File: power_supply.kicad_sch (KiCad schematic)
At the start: 46 parts, among them J3 JST_SH_1x4_SM04B-SRSS-TB-LF-SN, Q2 DMG1012T-7, U8 MPM54304GMN-0001, U9 LT3033EUDC_QFN

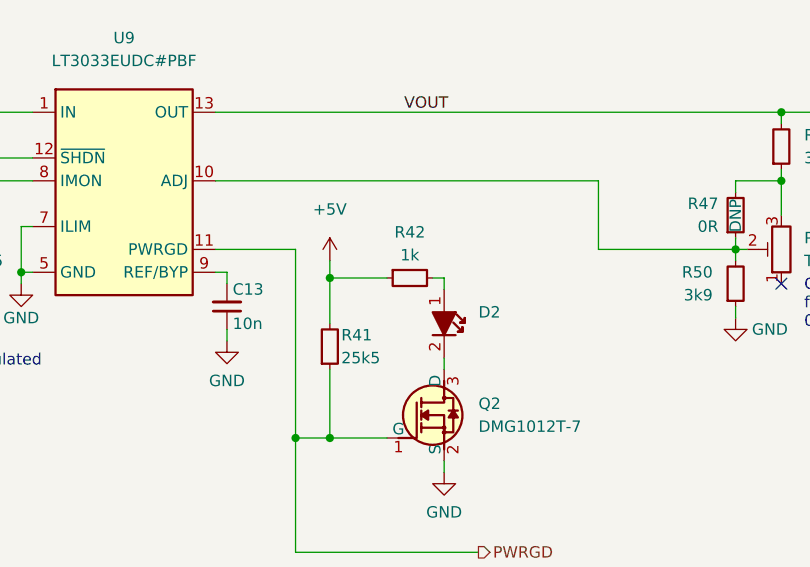
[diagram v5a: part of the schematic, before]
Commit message: [#52835] schematics: update translators pinout to for better package breakout
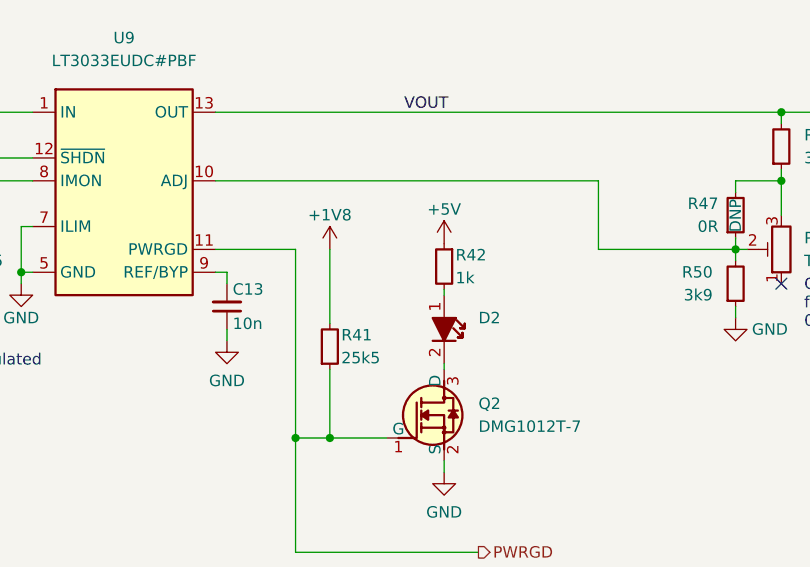
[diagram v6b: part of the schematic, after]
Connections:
- net +1V8: now also R41.2
- net +5V: no longer R41.2
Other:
- moved on the sheet: D2, R42
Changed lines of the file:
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@@
   (junction (at 189.23 186.055) (diameter 0) (color 0 0 0 0)
   )
-  (junction (at 231.14 196.85) (diameter 0) (color 0 0 0 0)
-  )
   (junction (at 241.3 78.74) (diameter 0) (color 0 0 0 0)
   )
@@
     (stroke (width 0) (type default) (color 0 0 0 0))
   )
-  (wire (pts (xy 231.14 194.945) (xy 231.14 196.85))
-    (stroke (width 0) (type default) (color 0 0 0 0))
-  )
   (wire (pts (xy 245.11 104.14) (xy 254 104.14))
     (stroke (width 0) (type default) (color 0 0 0 0))
@@
     (stroke (width 0) (type default) (color 0 0 0 0))
   )
-  (wire (pts (xy 242.57 196.85) (xy 243.84 196.85))
-    (stroke (width 0) (type default) (color 0 0 0 0))
-  )
   (polyline (pts (xy 229.235 55.245) (xy 229.235 66.675))
     (stroke (width 0) (type default) (color 0 0 0 0))
@@
     (stroke (width 0) (type default) (color 0 0 0 0))
   )
-  (wire (pts (xy 231.14 196.85) (xy 237.49 196.85))
-    (stroke (width 0) (type default) (color 0 0 0 0))
-  )
   (wire (pts (xy 180.975 57.785) (xy 180.975 59.055))
     (stroke (width 0) (type default) (color 0 0 0 0))
@@
     (stroke (width 0) (type default) (color 0 0 0 0))
   )
+  (wire (pts (xy 231.14 193.675) (xy 231.14 201.93))
+    (stroke (width 0) (type default) (color 0 0 0 0))
+  )
   (wire (pts (xy 302.26 178.435) (xy 327.66 178.435))
     (stroke (width 0) (type default) (color 0 0 0 0))
@@
     (stroke (width 0) (type default) (color 0 0 0 0))
   )
-  (wire (pts (xy 243.84 205.74) (xy 243.84 207.01))
+  (wire (pts (xy 243.84 206.375) (xy 243.84 207.01))
     (stroke (width 0) (type default) (color 0 0 0 0))
   )
@@
     (stroke (width 0) (type default) (color 0 0 0 0))
   )
-  (wire (pts (xy 231.14 196.85) (xy 231.14 201.93))
-    (stroke (width 0) (type default) (color 0 0 0 0))
-  )
   (wire (pts (xy 193.04 97.79) (xy 194.31 97.79))
     (stroke (width 0) (type default) (color 0 0 0 0))
@@
     (stroke (width 0) (type default) (color 0 0 0 0))
   )
-  (wire (pts (xy 243.84 196.85) (xy 243.84 198.12))
+  (wire (pts (xy 243.84 198.12) (xy 243.84 198.755))
     (stroke (width 0) (type default) (color 0 0 0 0))
   )
@@
     (pin "1")
   )
-  (symbol (lib_id "antmicropower:+5V") (at 231.14 194.945 0) (unit 1)
-    (in_bom yes) (on_board yes) (fields_autoplaced)
-    (property "Reference" "#PWR0212" (id 0) (at 246.38 197.485 0)
+  (symbol (lib_id "antmicropower:+5V") (at 243.84 193.04 0) (unit 1)
+    (in_bom yes) (on_board yes)
+    (property "Reference" "#PWR0212" (id 0) (at 259.08 195.58 0)
       (effects (font (size 1.27 1.27) (thickness 0.15)) (justify left bottom) hide)
     )
-    (property "Value" "+5V" (id 1) (at 231.14 189.23 0)
+    (property "Value" "+5V" (id 1) (at 243.84 189.23 0)
       (effects (font (size 1.27 1.27) (thickness 0.15)))
     )
-    (property "Footprint" "" (id 2) (at 246.38 202.565 0)
+    (property "Footprint" "" (id 2) (at 259.08 200.66 0)
       (effects (font (size 1.27 1.27) (thickness 0.15)) (justify left bottom) hide)
     )
-    (property "Datasheet" "" (id 3) (at 246.38 205.105 0)
+    (property "Datasheet" "" (id 3) (at 259.08 203.2 0)
       (effects (font (size 1.27 1.27) (thickness 0.15)) (justify left bottom) hide)
     )
-    (property "Author" "Antmicro" (id 4) (at 246.38 202.565 0)
+    (property "Author" "Antmicro" (id 4) (at 259.08 200.66 0)
       (effects (font (size 1.27 1.27) (thickness 0.15)) (justify left bottom) hide)
     )
-    (property "License" "Apache-2.0" (id 5) (at 246.38 205.105 0)
+    (property "License" "Apache-2.0" (id 5) (at 259.08 203.2 0)
       (effects (font (size 1.27 1.27) (thickness 0.15)) (justify left bottom) hide)
     )
@@
     (pin "1")
   )
-  (symbol (lib_id "antmicroLEDIndicationDiscrete:LED_G_0603_KP-1608CGCK") (at 243.84 198.12 270) (unit 1)
+  (symbol (lib_id "antmicroLEDIndicationDiscrete:LED_G_0603_KP-1608CGCK") (at 243.84 198.755 270) (unit 1)
     (in_bom yes) (on_board yes) (fields_autoplaced)
-    (property "Reference" "D2" (id 0) (at 247.65 200.6599 90)
+    (property "Reference" "D2" (id 0) (at 247.65 201.2949 90)
       (effects (font (size 1.27 1.27) (thickness 0.15)) (justify left))
     )
-    (property "Value" "LED_G_0603_KP-1608CGCK" (id 1) (at 247.65 203.1999 90)
+    (property "Value" "LED_G_0603_KP-1608CGCK" (id 1) (at 247.65 203.8349 90)
       (effects (font (size 1.27 1.27) (thickness 0.15)) (justify left) hide)
     )
-    (property "Footprint" "antmicro-footprints:LED_0603_1608Metric_G" (id 2) (at 233.68 220.98 0)
+    (property "Footprint" "antmicro-footprints:LED_0603_1608Metric_G" (id 2) (at 233.68 221.615 0)
       (effects (font (size 1.27 1.27) (thickness 0.15)) (justify left bottom) hide)
     )
-    (property "Datasheet" "http://www.farnell.com/datasheets/2045956.pdf" (id 3) (at 231.14 220.98 0)
+    (property "Datasheet" "http://www.farnell.com/datasheets/2045956.pdf" (id 3) (at 231.14 221.615 0)
       (effects (font (size 1.27 1.27) (thickness 0.15)) (justify left bottom) hide)
     )
-    (property "MPN" "KP-1608CGCK" (id 4) (at 228.6 220.98 0)
+    (property "MPN" "KP-1608CGCK" (id 4) (at 228.6 221.615 0)
       (effects (font (size 1.27 1.27) (thickness 0.15)) (justify left bottom) hide)
     )
-    (property "Manufacturer" "Kingbright" (id 5) (at 226.06 220.98 0)
+    (property "Manufacturer" "Kingbright" (id 5) (at 226.06 221.615 0)
       (effects (font (size 1.27 1.27) (thickness 0.15)) (justify left bottom) hide)
     )
-    (property "Author" "Antmicro" (id 6) (at 223.52 220.98 0)
+    (property "Author" "Antmicro" (id 6) (at 223.52 221.615 0)
       (effects (font (size 1.27 1.27) (thickness 0.15)) (justify left bottom) hide)
     )
-    (property "License" "Apache-2.0" (id 7) (at 220.98 220.98 0)
+    (property "License" "Apache-2.0" (id 7) (at 220.98 221.615 0)
       (effects (font (size 1.27 1.27) (thickness 0.15)) (justify left bottom) hide)
     )
@@
     (pin "2")
   )
+  (symbol (lib_id "antmicropower:+1V8") (at 231.14 193.675 0) (unit 1)
+    (in_bom yes) (on_board yes)
+    (property "Reference" "#PWR0270" (id 0) (at 246.38 196.215 0)
+      (effects (font (size 1.27 1.27) (thickness 0.15)) (justify left bottom) hide)
+    )
+    (property "Value" "+1V8" (id 1) (at 231.14 189.865 0)
+      (effects (font (size 1.27 1.27) (thickness 0.15)))
+    )
+    (property "Footprint" "" (id 2) (at 246.38 201.295 0)
+      (effects (font (size 1.27 1.27) (thickness 0.15)) (justify left bottom) hide)
+    )
+    (property "Datasheet" "" (id 3) (at 246.38 203.835 0)
+      (effects (font (size 1.27 1.27) (thickness 0.15)) (justify left bottom) hide)
+    )
+    (property "Author" "Antmicro" (id 4) (at 246.38 201.295 0)
+      (effects (font (size 1.27 1.27) (thickness 0.15)) (justify left bottom) hide)
+    )
+    (property "License" "Apache-2.0" (id 5) (at 246.38 203.835 0)
+      (effects (font (size 1.27 1.27) (thickness 0.15)) (justify left bottom) hide)
+    )
+    (pin "1")
+  )
   (symbol (lib_id "antmicropower:GND") (at 180.975 64.135 0) (unit 1)
     (in_bom yes) (on_board yes)
@@
     (pin "2")
   )
-  (symbol (lib_id "antmicroResistors0402:R_1k_0402") (at 237.49 196.85 0) (unit 1)
+  (symbol (lib_id "antmicroResistors0402:R_1k_0402") (at 243.84 193.04 270) (unit 1)
     (in_bom yes) (on_board yes)
-    (property "Reference" "R42" (id 0) (at 240.03 191.77 0)
-      (effects (font (size 1.27 1.27) (thickness 0.15)))
+    (property "Reference" "R42" (id 0) (at 245.11 194.31 90)
+      (effects (font (size 1.27 1.27) (thickness 0.15)) (justify left))
     )
-    (property "Value" "R_1k_0402" (id 1) (at 257.81 209.55 0)
+    (property "Value" "R_1k_0402" (id 1) (at 231.14 213.36 0)
       (effects (font (size 1.27 1.27) (thickness 0.15)) (justify left bottom) hide)
     )
-    (property "Footprint" "antmicro-footprints:R_0402_1005Metric" (id 2) (at 257.81 212.09 0)
+    (property "Footprint" "antmicro-footprints:R_0402_1005Metric" (id 2) (at 228.6 213.36 0)
       (effects (font (size 1.27 1.27) (thickness 0.15)) (justify left bottom) hide)
     )
-    (property "Datasheet" "https://www.bourns.com/docs/product-datasheets/cr.pdf" (id 3) (at 257.81 214.63 0)
+    (property "Datasheet" "https://www.bourns.com/docs/product-datasheets/cr.pdf" (id 3) (at 226.06 213.36 0)
       (effects (font (size 1.27 1.27) (thickness 0.15)) (justify left bottom) hide)
     )
-    (property "MPN" "CR0402-FX-1001GLF" (id 4) (at 257.81 217.17 0)
+    (property "MPN" "CR0402-FX-1001GLF" (id 4) (at 223.52 213.36 0)
       (effects (font (size 1.27 1.27) (thickness 0.15)) (justify left bottom) hide)
     )
-    (property "Manufacturer" "Bourns" (id 5) (at 257.81 219.71 0)
+    (property "Manufacturer" "Bourns" (id 5) (at 220.98 213.36 0)
       (effects (font (size 1.27 1.27) (thickness 0.15)) (justify left bottom) hide)
     )
-    (property "License" "Apache-2.0" (id 6) (at 257.81 222.25 0)
+    (property "License" "Apache-2.0" (id 6) (at 218.44 213.36 0)
       (effects (font (size 1.27 1.27) (thickness 0.15)) (justify left bottom) hide)
     )
-    (property "Author" "Antmicro" (id 7) (at 257.81 224.79 0)
+    (property "Author" "Antmicro" (id 7) (at 215.9 213.36 0)
       (effects (font (size 1.27 1.27) (thickness 0.15)) (justify left bottom) hide)
     )
-    (property "Val" "1k" (id 8) (at 240.03 194.31 0)
-      (effects (font (size 1.27 1.27) (thickness 0.15)))
+    (property "Val" "1k" (id 8) (at 245.11 196.85 90)
+      (effects (font (size 1.27 1.27) (thickness 0.15)) (justify left))
     )
-    (property "Tolerance" "1%" (id 9) (at 257.81 207.01 0)
+    (property "Tolerance" "1%" (id 9) (at 233.68 213.36 0)
       (effects (font (size 1.27 1.27)) (justify left bottom) hide)
     )

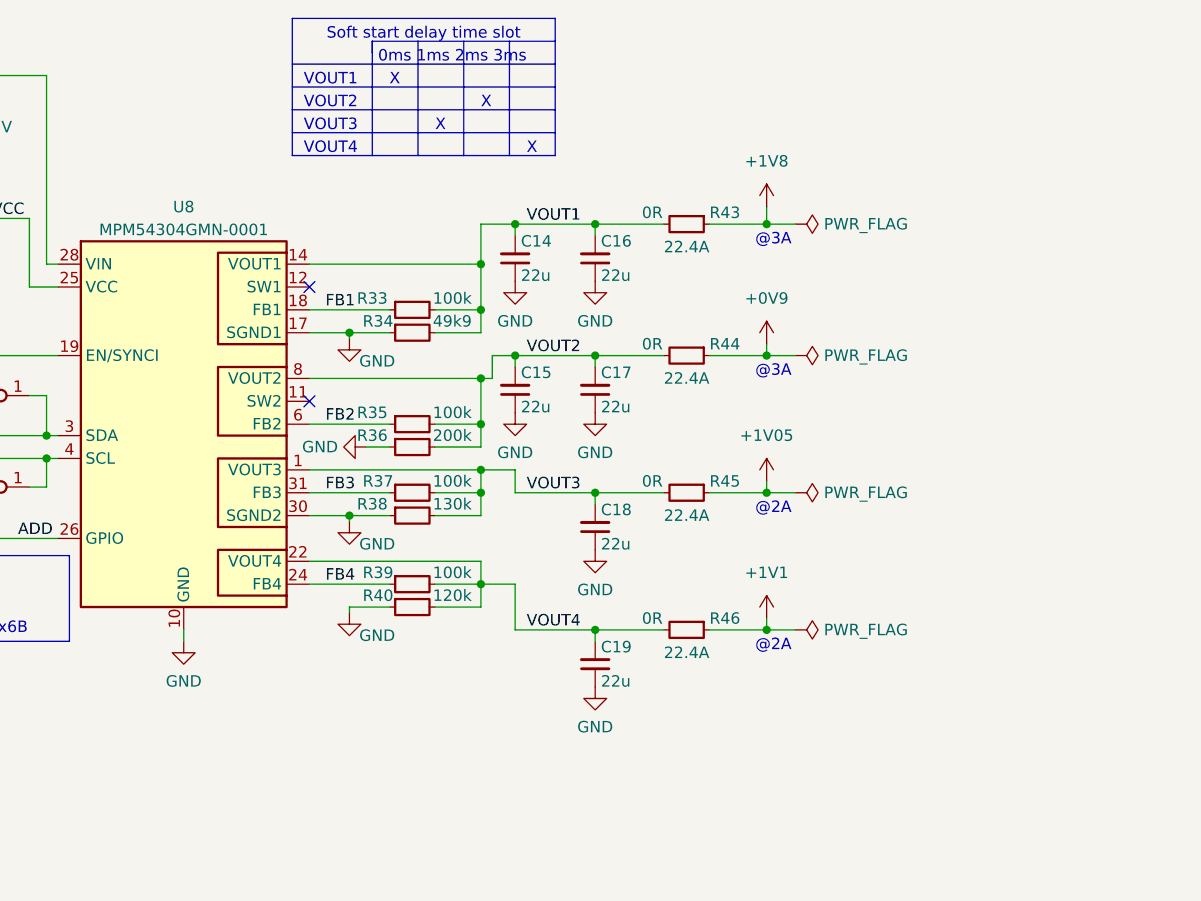
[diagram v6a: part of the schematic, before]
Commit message: [#52536] schematics: fix DCDC feedback resistors connection
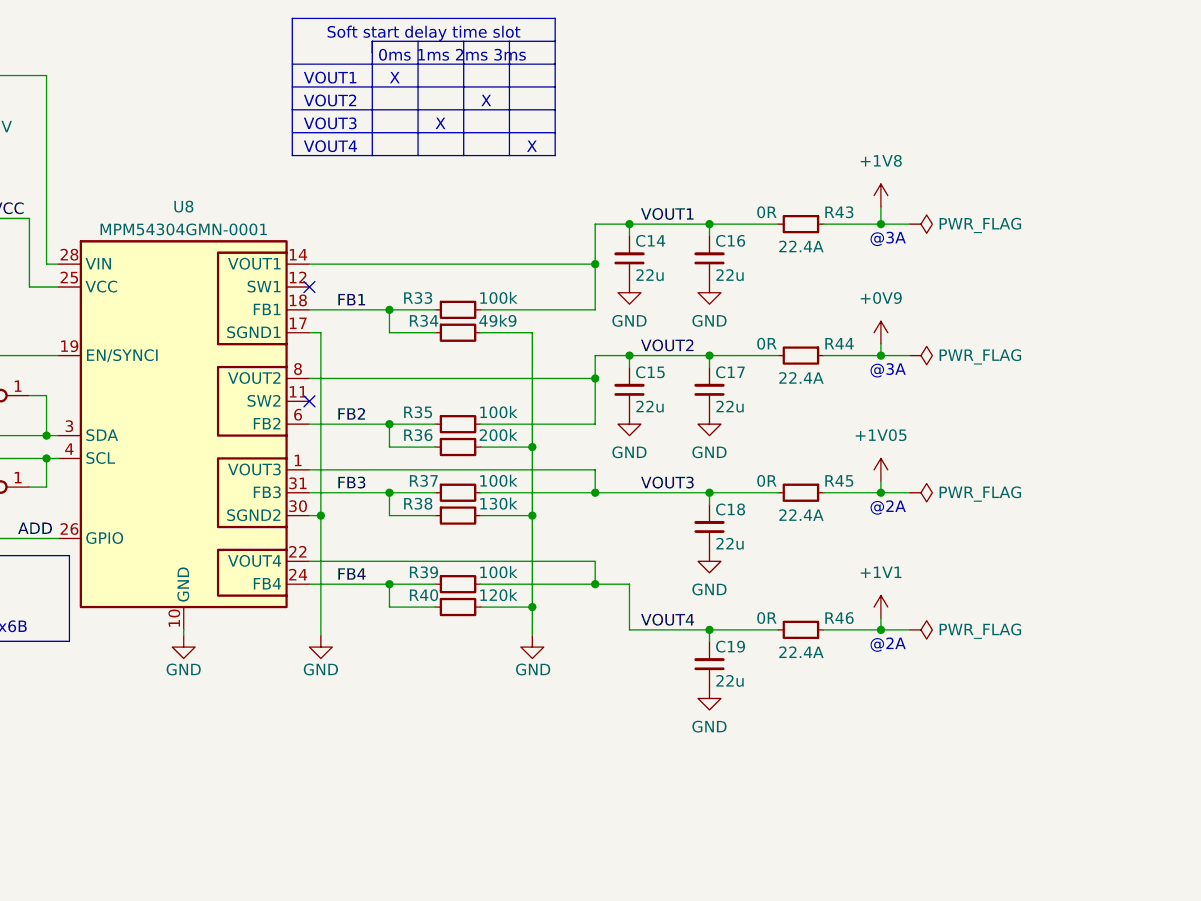
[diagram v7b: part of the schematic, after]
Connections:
- net FB1: now also R34.1
- net FB2: now also R36.1
- net FB3: now also R38.1
- net FB4: now also R40.1
- net GND: now also R34.2, R36.2, R38.2, R40.2; no longer R34.1, R36.1, R38.1, R40.1
- net VOUT1: no longer R34.2
- net VOUT2: no longer R36.2
- net VOUT3: no longer R38.2
- net VOUT4: no longer R40.2
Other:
- moved on the sheet: C14, C15, C16, C17, C18, C19, R33, R34, R35, R36, R37, R38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
